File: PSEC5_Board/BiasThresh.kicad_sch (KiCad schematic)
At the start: 24 parts

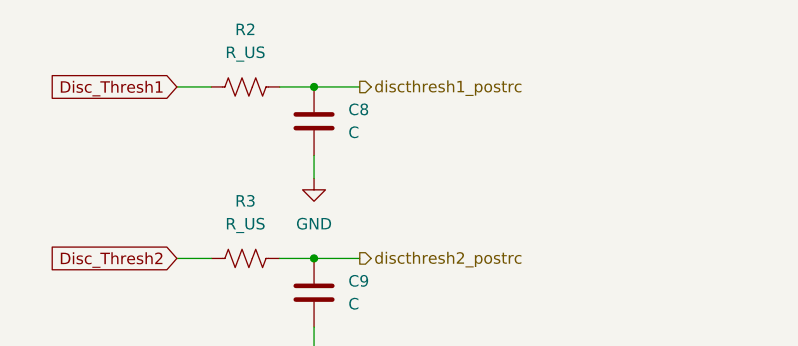
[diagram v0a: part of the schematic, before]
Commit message: Strain Relief
Added mounting holes.
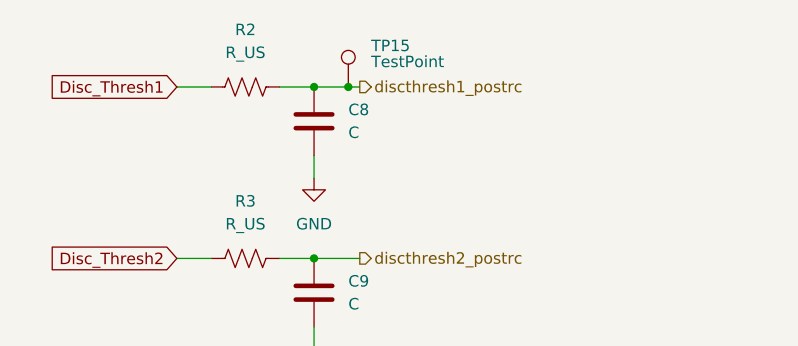
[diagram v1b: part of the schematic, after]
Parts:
- added TP15: TestPoint, TestPoint:TestPoint_THTPad_1.0x1.0mm_Drill0.5mm, symbol Connector:TestPoint
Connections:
- net discthresh1_postrc: now also TP15.1
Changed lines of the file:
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@@
+	)
+	(junction
+		(at 49.53 22.86)
+		(diameter 0)
+		(color 0 0 0 0)
 	)
 	(junction
@@
 	(wire
 		(pts
+			(xy 49.53 22.86) (xy 50.8 22.86)
+		)
+		(stroke
+			(width 0)
+			(type default)
+		)
+	)
+	(wire
+		(pts
 			(xy 46.99 161.29) (xy 46.99 163.83)
 		)
@@
 	(wire
 		(pts
-			(xy 45.72 22.86) (xy 50.8 22.86)
+			(xy 45.72 22.86) (xy 49.53 22.86)
 		)
 		(stroke
@@
 					(unit 1)
 				)
+			)
+		)
+	)
+	(symbol
+		(lib_id "Connector:TestPoint")
+		(at 49.53 22.86 0)
+		(unit 1)
+		(exclude_from_sim no)
+		(in_bom yes)
+		(on_board yes)
+		(dnp no)
+		(property "Reference" "TP15"
+			(at 52.07 18.2879 0)
+			(effects
+				(font
+					(size 1.27 1.27)
+				)
+				(justify left)
+			)
+		)
+		(property "Value" "TestPoint"
+			(at 52.07 20.066 0)
+			(effects
+				(font
+					(size 1.27 1.27)
+				)
+				(justify left)
+			)
+		)
+		(property "Footprint" "TestPoint:TestPoint_THTPad_1.0x1.0mm_Drill0.5mm"
+			(at 54.61 22.86 0)
+			(effects
+				(font
+					(size 1.27 1.27)
+				)
+				(hide yes)
+			)
+		)
+		(property "Datasheet" "~"
+			(at 54.61 22.86 0)
+			(effects
+				(font
+					(size 1.27 1.27)
+				)
+				(hide yes)
+			)
+		)
+		(property "Description" "test point"
+			(at 49.53 22.86 0)
+			(effects
+				(font
+					(size 1.27 1.27)
+				)
+				(hide yes)
+			)
+		)
+		(pin "1"
+		)
+		(instances
+			(project "PSEC5_Board"
+				(path "/af906810-6e6b-406e-b884-20eae48a7386/5d36e410-855a-42d4-b6a1-2e177315192b"
+					(reference "TP15")
+					(unit 1)
+				)

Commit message: Gerbers
Final push before first submission
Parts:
- renumbered TP15 to THRESH1
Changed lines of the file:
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@@
 		(on_board yes)
 		(dnp no)
-		(property "Reference" "TP15"
+		(property "Reference" "THRESH1"
 			(at 52.07 18.2879 0)
 			(effects
@@
 			(project "PSEC5_Board"
 				(path "/af906810-6e6b-406e-b884-20eae48a7386/5d36e410-855a-42d4-b6a1-2e177315192b"
-					(reference "TP15")
+					(reference "THRESH1")
 					(unit 1)
 				)
